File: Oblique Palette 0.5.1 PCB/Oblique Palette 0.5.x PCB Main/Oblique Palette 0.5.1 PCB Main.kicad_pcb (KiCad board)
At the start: 2 copper layers, 235 x 110 mm, 310 parts, among them J11 Conn_01x03_Male_Pin, J13 Conn_01x03_Male_Pin, J14 Conn_01x03_Male_Pin, J15 Conn_01x03_Male_Pin, J17 AudioJack2_SwitchT, J18 Conn_01x03_Male_Pin, J2 Conn_01x03_Male_Pin, J20 AudioJack2_SwitchT, J21 Conn_01x03_Male_Pin, J23 AudioJack2_SwitchT, J24 Conn_01x03_Male_Pin, J26 AudioJack2_SwitchT, J27 Conn_01x03_Male_Pin, J29 AudioJack2_SwitchT, J30 Conn_01x03_Male_Pin, J32 AudioJack2_SwitchT, J33 Conn_01x03_Male_Pin, J35 AudioJack2_SwitchT, J36 Conn_01x03_Male_Pin, J38 AudioJack2_SwitchT, J39 Conn_01x02_Pin, J4 Conn_01x03_Male_Pin, J40 Conn_01x03_Female_Pin, J42 AudioJack2_SwitchT, J43 Conn_01x02_Pin, J44 Conn_01x03_Female_Pin, J46 AudioJack2_SwitchT, J47 Conn_01x02_Pin, J48 Conn_01x03_Female_Pin, J5 Conn_01x03_Male_Pin, J50 AudioJack2_SwitchT, J51 Conn_01x02_Pin, J52 Conn_01x03_Female_Pin, J54 AudioJack2_SwitchT, J55 Conn_01x02_Pin, J56 Conn_01x03_Female_Pin, J58 AudioJack2_SwitchT, J59 Conn_01x02_Pin, J60 Conn_01x03_Female_Pin, J62 AudioJack2_SwitchT, J63 Conn_01x02_Pin, J64 Conn_01x03_Female_Pin, J66 AudioJack2_SwitchT, J67 Conn_01x02_Pin, J68 Conn_01x03_Female_Pin, J7 Conn_01x03_Male_Pin, J70 AudioJack2_SwitchT, J71 Conn_01x03_Male_Pin, J72 Conn_01x02_Pin, J9 Conn_01x03_Male_Pin, U1 CD4051BM96, U10 MCP6004T-E/SL, U11 MCP4725A0T-E/CH, U12 MCP6004T-E/SL, U13 MCP4725A1T-E/CH, U14 MCP6004T-E/SL, U15 MCP4725A0T-E/CH, U16 MCP6004T-E/SL, U17 MCP4725A1T-E/CH, U18 MCP6004T-E/SL, U19 MCP4725A0T-E/CH, U2 Pico, U20 MCP6004T-E/SL, U21 MCP4725A1T-E/CH, U22 MCP6004T-E/SL, U23 MCP4725A0T-E/CH, U24 MCP6004T-E/SL, U25 MCP4725A1T-E/CH, U26 MCP6004T-E/SL, U3 MCP6004T-E/SL, U4 MCP6004T-E/SL, U5 MCP6004T-E/SL, U6 MCP6004T-E/SL, U7 MCP6004T-E/SL, U8 MCP6004T-E/SL, U9 MCP6004T-E/SL

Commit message: All traces(?) now connected on PCB.
This is looking good to me. Vcc and VServo are merged for simplicity. Not the best solution. I think maybe a breakable trace or a single jumper might be the way to do this.
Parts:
- removed J15, J18, J21, J24, J27, J30, J33, J36: Conn_01x03_Male_Pin, Connector_PinHeader_2.54mm:PinHeader_1x03_P2.54mm_Vertical
- added J16: Conn_01x03_Female_Pin, Connector_PinSocket_2.54mm:PinSocket_1x03_P2.54mm_Vertical, F.Cu at (40.6, 60.4)
- added J19: Conn_01x03_Female_Pin, Connector_PinSocket_2.54mm:PinSocket_1x03_P2.54mm_Vertical, F.Cu at (68.0, 60.4)
- added J22: Conn_01x03_Female_Pin, Connector_PinSocket_2.54mm:PinSocket_1x03_P2.54mm_Vertical, F.Cu at (96.0, 60.4)
- added J25: Conn_01x03_Female_Pin, Connector_PinSocket_2.54mm:PinSocket_1x03_P2.54mm_Vertical, F.Cu at (123.5, 60.6)
- added J28: Conn_01x03_Female_Pin, Connector_PinSocket_2.54mm:PinSocket_1x03_P2.54mm_Vertical, F.Cu at (151.0, 60.4)
- added J31: Conn_01x03_Female_Pin, Connector_PinSocket_2.54mm:PinSocket_1x03_P2.54mm_Vertical, F.Cu at (179.0, 60.4)
- added J34: Conn_01x03_Female_Pin, Connector_PinSocket_2.54mm:PinSocket_1x03_P2.54mm_Vertical, F.Cu at (206.5, 60.4)
- added J37: Conn_01x03_Female_Pin, Connector_PinSocket_2.54mm:PinSocket_1x03_P2.54mm_Vertical, F.Cu at (234.0, 60.4)
- added R160: 200K, Resistor_SMD:R_0805_2012Metric, F.Cu at (41.1, 55.6)
- added R161: 200K, Resistor_SMD:R_0805_2012Metric, F.Cu at (68.6, 55.4)
- added R162: 200K, Resistor_SMD:R_0805_2012Metric, F.Cu at (96.6, 55.4)
- added R163: 200K, Resistor_SMD:R_0805_2012Metric, F.Cu at (124.5, 54.8)
- added R164: 200K, Resistor_SMD:R_0805_2012Metric, F.Cu at (151.6, 54.9)
- added R165: 200K, Resistor_SMD:R_0805_2012Metric, F.Cu at (179.5, 55.1)
- added R166: 200K, Resistor_SMD:R_0805_2012Metric, F.Cu at (207.1, 55.0)
- added R167: 200K, Resistor_SMD:R_0805_2012Metric, F.Cu at (234.9, 55.4)
- R101, R105, R68, R72, R79, R83, R90, R94: value 1K -> 100K
- R13, R15, R21, R23, R29, R31, R37, R39, R45, R47, R5, R53, R55, R61, R63, R7: value 128R -> 127R
- U1: value CD4051BM96 -> CD4051B
- U10, U12, U14, U16, U18, U20, U22, U24, U26, U3, U4, U5, U6, U7, U8, U9: value MCP6004T-E/SL -> MCP6004
- U11, U15, U19, U23: value MCP4725A0T-E/CH -> MCP4725xxx-xCH
- U13, U17, U21, U25: value MCP4725A1T-E/CH -> MCP4725xxx-xCH
- moved R6 27.1 mm to (20.0, 37.8), turned to 90 degrees
- moved R7 25.2 mm to (27.5, 60.9), turned to 0 degrees
- moved R5 14.6 mm to (27.5, 54.9), turned to 0 degrees
- moved R4 4.99 mm to (20.0, 42.9), turned to 90 degrees
- moved R3 3.00 mm to (27.5, 57.9)
- moved C9 2.51 mm to (42.0, 26.9)
- moved C10 2.50 mm to (69.7, 26.4)
- moved C11 2.50 mm to (97.3, 26.4)
- moved C12 2.50 mm to (125.0, 26.4)
- moved C13 2.50 mm to (152.7, 26.4)
- moved C14 2.50 mm to (180.3, 26.4)
- moved C15 2.50 mm to (208.0, 26.4)
- moved C16 2.50 mm to (235.6, 26.4)
- moved U1 0.44 mm to (123.6, 73.4)
- turned R12 to 90 degrees
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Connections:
- net ADC_0 renamed Net-(U1-A)
- net ADC_1 renamed Net-(U1-B)
- net ADC_2 renamed Net-(U1-C)
- U1 pad 1: /ANALOG_IN_1 -> /Input 5/ANALOG_CHANNEL
- U1 pad 12: /ANALOG_IN_4 -> /Input 4/ANALOG_CHANNEL
- U1 pad 13: /ANALOG_IN_3 -> /Input 1/ANALOG_CHANNEL
- U1 pad 14: /ANALOG_IN_6 -> /Input 2/ANALOG_CHANNEL
- U1 pad 15: /ANALOG_IN_5 -> /Input 3/ANALOG_CHANNEL
- U1 pad 2: /ANALOG_IN_7 -> /Input 7/ANALOG_CHANNEL
- U1 pad 3: ADC -> Net-(U1-X)
- U1 pad 4: /ANALOG_IN -> /Input 8/ANALOG_CHANNEL
- U1 pad 5: /ANALOG_IN_2 -> /Input 6/ANALOG_CHANNEL
- U10 pad 1: /Input 8/ANALOG_PIN -> /Input 8/ANALOG_CHANNEL
- U10 pad 2: /Input 8/ANALOG_PIN -> /Input 8/ANALOG_CHANNEL
- U2 pad 34: ANALOG_PIN -> Net-(U1-X)
- U3 pad 1: /Input 1/ANALOG_PIN -> /Input 1/ANALOG_CHANNEL
- U3 pad 2: /Input 1/ANALOG_PIN -> /Input 1/ANALOG_CHANNEL
- U4 pad 1: /Input 2/ANALOG_PIN -> /Input 2/ANALOG_CHANNEL
- U4 pad 2: /Input 2/ANALOG_PIN -> /Input 2/ANALOG_CHANNEL
- U5 pad 1: /Input 3/ANALOG_PIN -> /Input 3/ANALOG_CHANNEL
- U5 pad 2: /Input 3/ANALOG_PIN -> /Input 3/ANALOG_CHANNEL
- U6 pad 1: /Input 4/ANALOG_PIN -> /Input 4/ANALOG_CHANNEL
- U6 pad 2: /Input 4/ANALOG_PIN -> /Input 4/ANALOG_CHANNEL
- U7 pad 1: /Input 5/ANALOG_PIN -> /Input 5/ANALOG_CHANNEL
- U7 pad 2: /Input 5/ANALOG_PIN -> /Input 5/ANALOG_CHANNEL
- U8 pad 1: /Input 6/ANALOG_PIN -> /Input 6/ANALOG_CHANNEL
- U8 pad 2: /Input 6/ANALOG_PIN -> /Input 6/ANALOG_CHANNEL
- U9 pad 1: /Input 7/ANALOG_PIN -> /Input 7/ANALOG_CHANNEL
- U9 pad 2: /Input 7/ANALOG_PIN -> /Input 7/ANALOG_CHANNEL
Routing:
- net GNDREF: track 0.00 -> 2072.2 mm, vias 0 -> 14
- net V_SERVO: track 0.00 -> 1449.1 mm, vias 0 -> 14
- net +3.3V: track 0.00 -> 520.5 mm, vias 0 -> 18
- net SDA_0: track 0.00 -> 283.8 mm, vias 0 -> 7
- net SCL_0: track 0.00 -> 247.8 mm, vias 0 -> 8
- net Net-(J37-Pin_1): track 0.00 -> 240.1 mm, vias 0 -> 2
- net SERVO_1: track 0.00 -> 232.1 mm, vias 0 -> 1
- net Net-(U10A-+): track 0.00 -> 211.0 mm, vias 0 -> 3
- net Net-(J31-Pin_1): track 0.00 -> 207.5 mm, vias 0 -> 3
- net SERVO_2: track 0.00 -> 206.4 mm, vias 0 -> 1
- net Net-(J34-Pin_1): track 0.00 -> 185.0 mm, vias 0 -> 2
- net Net-(J25-Pin_1): track 0.00 -> 183.4 mm, vias 0 -> 2
- net SERVO_3: track 0.00 -> 180.1 mm, vias 0 -> 1
- net Net-(U8A-+): track 0.00 -> 175.8 mm, vias 0 -> 4
- net Net-(J28-Pin_1): track 0.00 -> 169.2 mm, vias 0 -> 3
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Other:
- outline, holes or cut-outs redrawn
- board text added: "Emphasize differences."
- board text added: "palette prototype 0.5.4"
- board text removed: "Where does the edge of the frame start?"
- board text removed: "palette prototype 0.5.3"

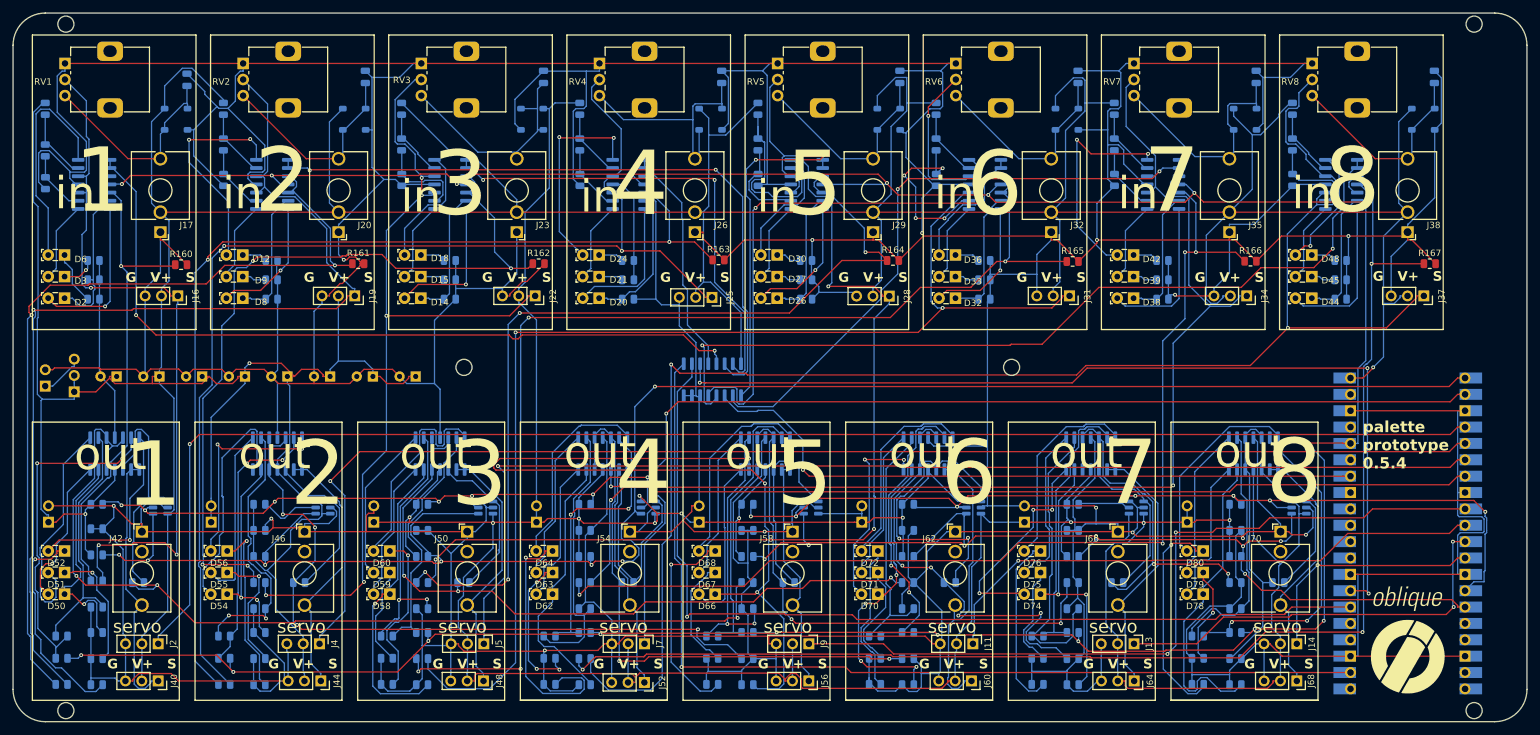
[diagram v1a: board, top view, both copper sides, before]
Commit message: I've cleaned up all sorts of misplaced resistors. Manually routing input channel 1 to replicate across inputs.
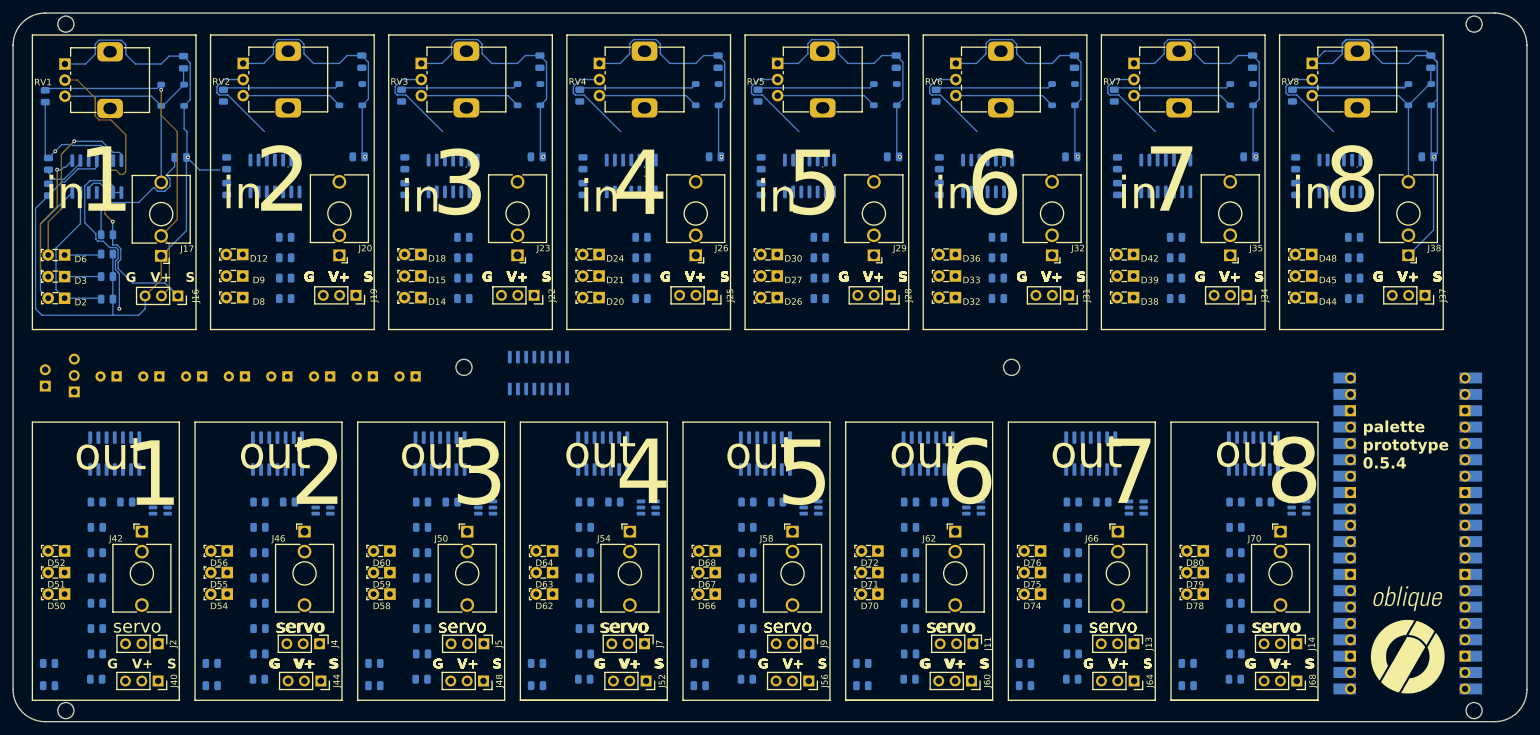
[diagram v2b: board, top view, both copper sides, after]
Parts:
- removed J39, J43, J47, J51, J55, J59, J63, J67: Conn_01x02_Pin, Connector_PinHeader_2.54mm:PinHeader_1x02_P2.54mm_Vertical
- R160, R161, R162, R163, R164, R165, R166, R167: moved to B.Cu
- moved R105 136.2 mm to (223.2, 51.3)
- moved R94 110.7 mm to (167.9, 51.3)
- moved R101 106.3 mm to (195.5, 51.3)
- moved R112 101.0 mm to (28.0, 104.2), turned to 0 degrees
- moved R83 94.9 mm to (112.6, 51.3)
- moved R90 81.7 mm to (140.2, 51.3)
- moved R72 77.6 mm to (57.2, 51.3)
- moved R116 76.8 mm to (53.2, 104.2), turned to 0 degrees
- moved R123 75.4 mm to (78.5, 104.2), turned to 0 degrees
- moved R79 62.2 mm to (84.9, 51.3)
- moved R68 53.8 mm to (29.6, 50.9)
- moved R127 51.7 mm to (103.8, 104.2), turned to 0 degrees
- moved R134 50.5 mm to (129.0, 104.2), turned to 0 degrees
- moved R138 28.2 mm to (154.2, 104.2), turned to 0 degrees
- moved U1 27.0 mm to (96.6, 72.4)
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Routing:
- net GNDREF: track 2072.2 -> 467.3 mm, vias 14 -> 8
- net V_SERVO: track 1449.1 -> 201.2 mm, vias 14 -> 1
- net +3.3V: track 520.5 -> 0.00 mm, vias 18 -> 0
- net SDA_0: track 283.8 -> 0.00 mm, vias 7 -> 0
- net SCL_0: track 247.8 -> 0.00 mm, vias 8 -> 0
- net SERVO_1: track 232.1 -> 0.00 mm, vias 1 -> 0
- net Net-(J37-Pin_1): track 240.1 -> 15.4 mm, vias 2 -> 0
- net Net-(U10A-+): track 211.0 -> 1.01 mm, vias 3 -> 0
- net SERVO_2: track 206.4 -> 0.00 mm, vias 1 -> 0
- net Net-(J31-Pin_1): track 207.5 -> 15.4 mm, vias 3 -> 0
- net SERVO_3: track 180.1 -> 0.00 mm, vias 1 -> 0
- net Net-(U8A-+): track 175.8 -> 1.01 mm, vias 4 -> 0
- net Net-(J34-Pin_1): track 185.0 -> 15.4 mm, vias 2 -> 0
- net Net-(J25-Pin_1): track 183.4 -> 15.4 mm, vias 2 -> 0
- net Net-(U9A-+): track 167.4 -> 1.01 mm, vias 4 -> 0
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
